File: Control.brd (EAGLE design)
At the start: 93.7 x 34.3 mm, 23 parts, among them IC1 MEGA8-P, Q1 16MHz, T1 2N2222, X1 MKDSN1,5/3-5,08, X2 MKDSN1,5/3-5,08

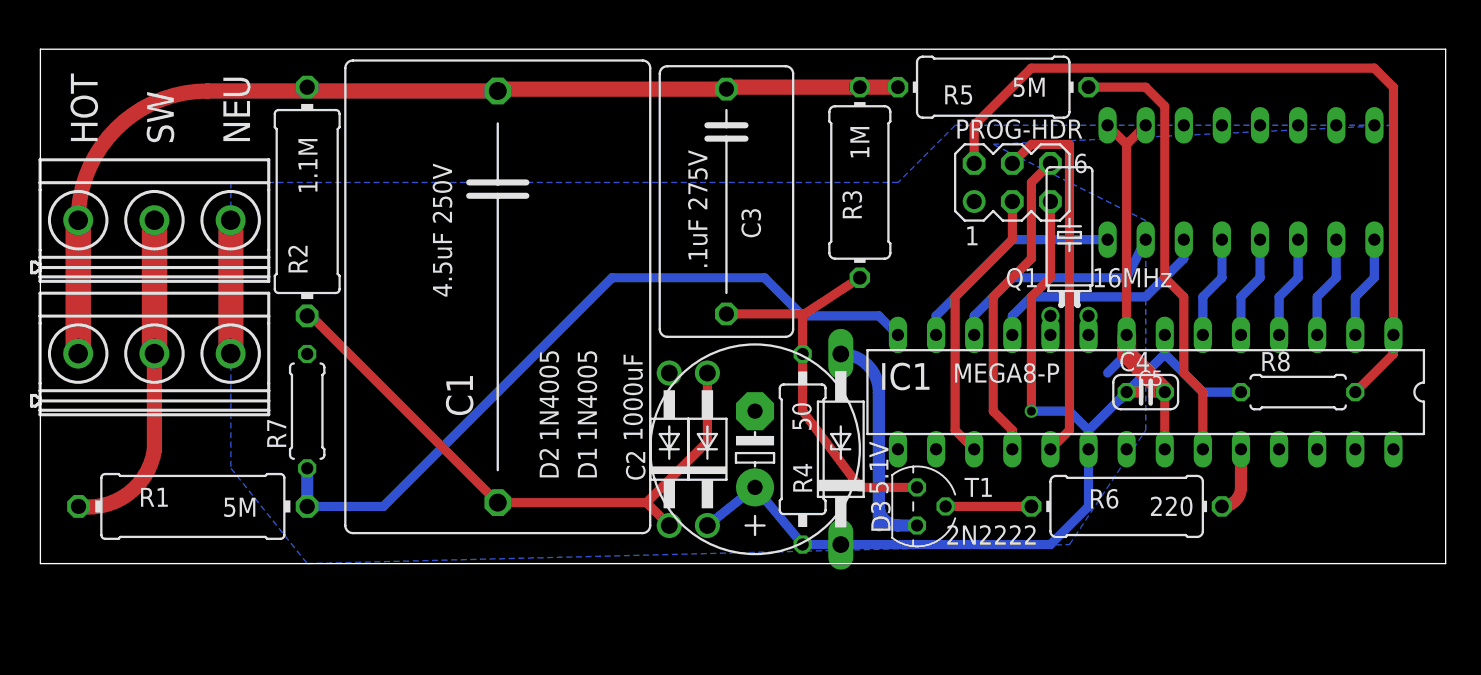
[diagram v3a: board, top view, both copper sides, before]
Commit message: Added surface mount options for low voltage section
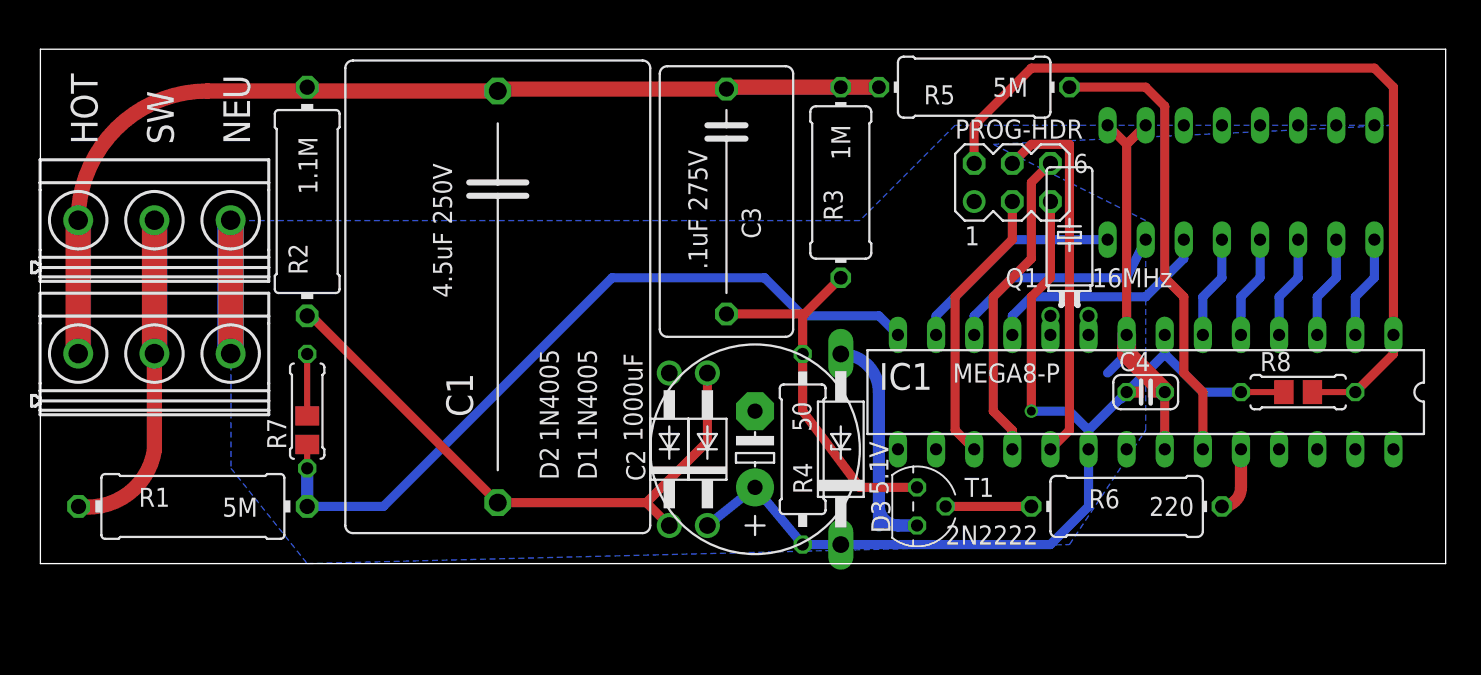
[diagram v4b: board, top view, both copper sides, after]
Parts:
- added R10, R9: 120K, rcl:M0805
- moved R3 1.27 mm to (59.7, 25.4)
- moved R5 1.27 mm to (68.6, 31.8)
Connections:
- net +5V: now also R9.1
- net GND: now also R10.2
- net N$18: now also R10.1
- net N$8: now also R9.2
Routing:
- net GND: track 43.6 -> 56.6 mm
- net N$8: track 54.0 -> 56.8 mm
- net +5V: track 68.5 -> 71.4 mm
- net N$18: track 49.8 -> 51.4 mm
- net N$3: track 67.2 -> 65.9 mm
- net N$21: track 29.5 -> 30.8 mm
- net N$19: track 26.2 -> 25.3 mm
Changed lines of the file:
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@@
 <attribute name="VALUE" x="66.675" y="1.27" size="1.27" layer="25" ratio="10"/>
 </element>
-<element name="R3" library="rcl" package="0411/12" value="1M" x="60.96" y="25.4" smashed="yes" rot="R90">
-<attribute name="NAME" x="61.087" y="22.86" size="1.27" layer="25" ratio="10" rot="R90"/>
-<attribute name="VALUE" x="61.595" y="26.8986" size="1.27" layer="25" ratio="10" rot="R90"/>
+<element name="R3" library="rcl" package="0411/12" value="1M" x="59.69" y="25.4" smashed="yes" rot="R90">
+<attribute name="NAME" x="59.817" y="22.86" size="1.27" layer="25" ratio="10" rot="R90"/>
+<attribute name="VALUE" x="60.325" y="26.8986" size="1.27" layer="25" ratio="10" rot="R90"/>
 </element>
 <element name="R4" library="rcl" package="0309/12" value="50" x="57.15" y="7.62" smashed="yes" rot="R270">
@@
 <attribute name="VALUE" x="56.4642" y="10.795" size="1.27" layer="25" ratio="10" rot="R270"/>
 </element>
-<element name="R5" library="rcl" package="0411/12" value="5M" x="69.85" y="31.75" smashed="yes" rot="R180">
-<attribute name="NAME" x="68.58" y="31.877" size="1.27" layer="25" ratio="10" rot="R180"/>
-<attribute name="VALUE" x="73.4314" y="32.385" size="1.27" layer="25" ratio="10" rot="R180"/>
+<element name="R5" library="rcl" package="0411/12" value="5M" x="68.58" y="31.75" smashed="yes" rot="R180">
+<attribute name="NAME" x="67.31" y="31.877" size="1.27" layer="25" ratio="10" rot="R180"/>
+<attribute name="VALUE" x="72.1614" y="32.385" size="1.27" layer="25" ratio="10" rot="R180"/>
 </element>
 <element name="C3" library="rcl" package="C150-091X182" value=".1uF 275V" x="52.07" y="24.13" smashed="yes" rot="R270">
@@
 </element>
 <element name="C4" library="rcl" package="C025-024X044" value="" x="80.01" y="11.43"/>
-<element name="R7" library="rcl" package="0207/7" value="120K" x="24.13" y="10.16" rot="R90"/>
+<element name="R7" library="rcl" package="0207/7" value="120K" x="24.13" y="10.16" smashed="yes" rot="R90">
+<attribute name="NAME" x="22.733" y="7.62" size="1.27" layer="25" ratio="10" rot="R90"/>
+</element>
 <element name="R8" library="rcl" package="0207/7" value="120K" x="90.17" y="11.43" smashed="yes">
 <attribute name="NAME" x="87.63" y="12.827" size="1.27" layer="25" ratio="10"/>
-<attribute name="VALUE" x="87.884" y="10.8712" size="1.27" layer="27" ratio="10"/>
-</element>
-<element name="C5" library="rcl" package="C0402K" value="" x="80.01" y="11.43"/>
+<attribute name="VALUE" x="87.884" y="8.89" size="1.27" layer="27" ratio="10"/>
+</element>
+<element name="C5" library="rcl" package="C0402K" value="" x="80.01" y="11.43" smashed="yes">
+<attribute name="VALUE" x="79.51" y="9.98" size="1.016" layer="27"/>
+</element>
+<element name="R9" library="rcl" package="M0805" value="120K" x="90.17" y="11.43" smashed="yes"/>
+<element name="R10" library="rcl" package="M0805" value="120K" x="24.13" y="8.89" smashed="yes" rot="R90">
+<attribute name="VALUE" x="26.67" y="7.62" size="1.27" layer="27" rot="R90"/>
+</element>
 </elements>
 <signals>
@@
 <wire x1="81.28" y1="7.62" x2="81.28" y2="11.43" width="0.6096" layer="1"/>
 <polygon width="1.016" layer="16" isolate="0.6096">
-<vertex x="19.05" y="25.4"/>
+<vertex x="19.05" y="22.86"/>
 <vertex x="19.05" y="6.35"/>
 <vertex x="24.13" y="0"/>
@@
 <vertex x="96.52" y="29.21"/>
 <vertex x="67.31" y="29.21"/>
-<vertex x="63.5" y="25.4"/>
+<vertex x="60.96" y="22.86"/>
 </polygon>
 <wire x1="78.74" y1="15.24" x2="78.74" y2="13.97" width="0.6096" layer="16"/>
@@
 <wire x1="78.74" y1="27.94" x2="80.01" y2="29.21" width="0.6096" layer="1"/>
 <contactref element="C5" pad="2"/>
+<wire x1="19.0289" y1="22.885" x2="19.0289" y2="13.995" width="1.778" layer="16"/>
+<contactref element="R10" pad="2"/>
+<wire x1="24.13" y1="9.84" x2="24.13" y2="13.97" width="0.4064" layer="1"/>
 <wire x1="81.28" y1="11.43" x2="80.61" y2="11.43" width="0" layer="19" extent="1-1"/>
 </signal>
@@
 <wire x1="93.98" y1="11.43" x2="96.52" y2="13.97" width="0.6096" layer="1"/>
 <wire x1="96.52" y1="13.97" x2="96.52" y2="15.24" width="0.6096" layer="1"/>
+<contactref element="R9" pad="2"/>
+<wire x1="91.12" y1="11.43" x2="93.98" y2="11.43" width="0.4064" layer="1"/>
 </signal>
 <signal name="+5V">
@@
 <wire x1="83.82" y1="11.43" x2="81.28" y2="13.97" width="0.6096" layer="16"/>
 <contactref element="C5" pad="1"/>
-<wire x1="78.74" y1="11.43" x2="79.41" y2="11.43" width="0" layer="19" extent="1-16"/>
+<contactref element="R9" pad="1"/>
+<wire x1="79.41" y1="11.43" x2="78.74" y2="11.43" width="0" layer="19" extent="1-16"/>
+<wire x1="86.36" y1="11.43" x2="89.22" y2="11.43" width="0.4064" layer="1"/>
 </signal>
 <signal name="N$9">
@@
 <contactref element="R7" pad="1"/>
 <wire x1="24.13" y1="3.81" x2="24.13" y2="6.35" width="0.8128" layer="16"/>
+<contactref element="R10" pad="1"/>
+<wire x1="24.13" y1="7.94" x2="24.13" y2="6.35" width="0.4064" layer="1"/>
 </signal>
 <signal name="N$19">
@@
 <wire x1="52.07" y1="16.637" x2="57.15" y2="16.637" width="0.6096" layer="1"/>
 <wire x1="57.15" y1="16.637" x2="57.277" y2="16.637" width="0.6096" layer="1"/>
-<wire x1="57.277" y1="16.637" x2="60.96" y2="19.05" width="0.6096" layer="1"/>
+<wire x1="57.277" y1="16.637" x2="59.69" y2="19.05" width="0.6096" layer="1"/>
 <wire x1="57.15" y1="13.97" x2="57.15" y2="16.637" width="0.6096" layer="1"/>
 <wire x1="57.15" y1="13.97" x2="57.15" y2="10.16" width="0.6096" layer="1"/>
@@
 <wire x1="36.957" y1="31.623" x2="52.07" y2="31.623" width="1.016" layer="1"/>
 <wire x1="52.07" y1="31.623" x2="52.197" y2="31.75" width="1.016" layer="1"/>
-<wire x1="52.197" y1="31.75" x2="60.96" y2="31.75" width="1.016" layer="1"/>
-<wire x1="60.96" y1="31.75" x2="63.5" y2="31.75" width="1.016" layer="1"/>
+<wire x1="52.197" y1="31.75" x2="59.69" y2="31.75" width="1.016" layer="1"/>
+<wire x1="59.69" y1="31.75" x2="62.23" y2="31.75" width="1.016" layer="1"/>
 <wire x1="17.4799" y1="31.496" x2="8.8689" y2="22.885" width="1.016" layer="1" curve="90"/>
 <wire x1="8.8689" y1="22.885" x2="8.8689" y2="13.995" width="1.6764" layer="1"/>
@@
 <wire x1="81.28" y1="19.05" x2="81.28" y2="30.48" width="0.6096" layer="1"/>
 <wire x1="81.28" y1="30.48" x2="80.01" y2="31.75" width="0.6096" layer="1"/>
-<wire x1="80.01" y1="31.75" x2="76.2" y2="31.75" width="0.6096" layer="1"/>
+<wire x1="80.01" y1="31.75" x2="74.93" y2="31.75" width="0.6096" layer="1"/>
 </signal>
 <signal name="N$22">

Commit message: Updated board - relocated programming header and large filter capacitor from DC block due to assembly dificulties stacking the filter capacitor on top of the diodes.
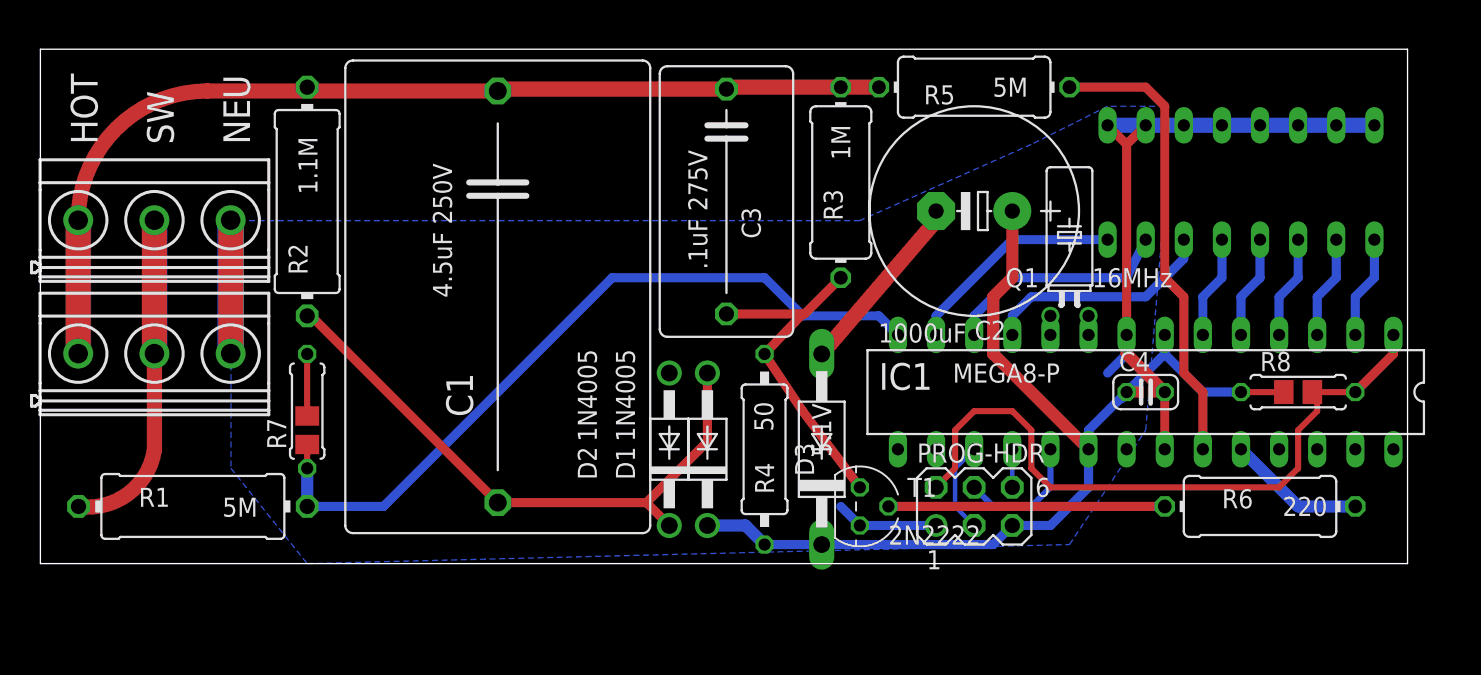
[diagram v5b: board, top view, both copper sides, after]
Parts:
- moved PROG-HDR 21.7 mm to (68.6, 3.81)
- moved C2 21.6 mm to (68.6, 23.5), turned to 180 degrees
- moved R6 8.89 mm to (87.6, 3.81)
- moved T1 3.81 mm to (61.0, 3.81)
- moved R4 2.54 mm to (54.6, 7.62)
- moved D3 1.27 mm to (58.4, 7.62)
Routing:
- net GND: track 56.6 -> 77.4 mm
- net N$6: track 21.2 -> 2.54 mm
- net N$7: track 25.2 -> 8.67 mm
- net N$5: track 5.72 -> 18.4 mm
- net N$9: track 18.6 -> 6.13 mm
- net N$8: track 56.8 -> 45.3 mm
- net N$22: track 4.34 -> 9.20 mm
- net +5V: track 71.4 -> 68.7 mm, vias 1 -> 0
- net N$19: track 25.3 -> 23.2 mm
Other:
- board size 93.7 x 34.3 mm -> 91.1 x 34.3 mm

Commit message: Slight board size reduction
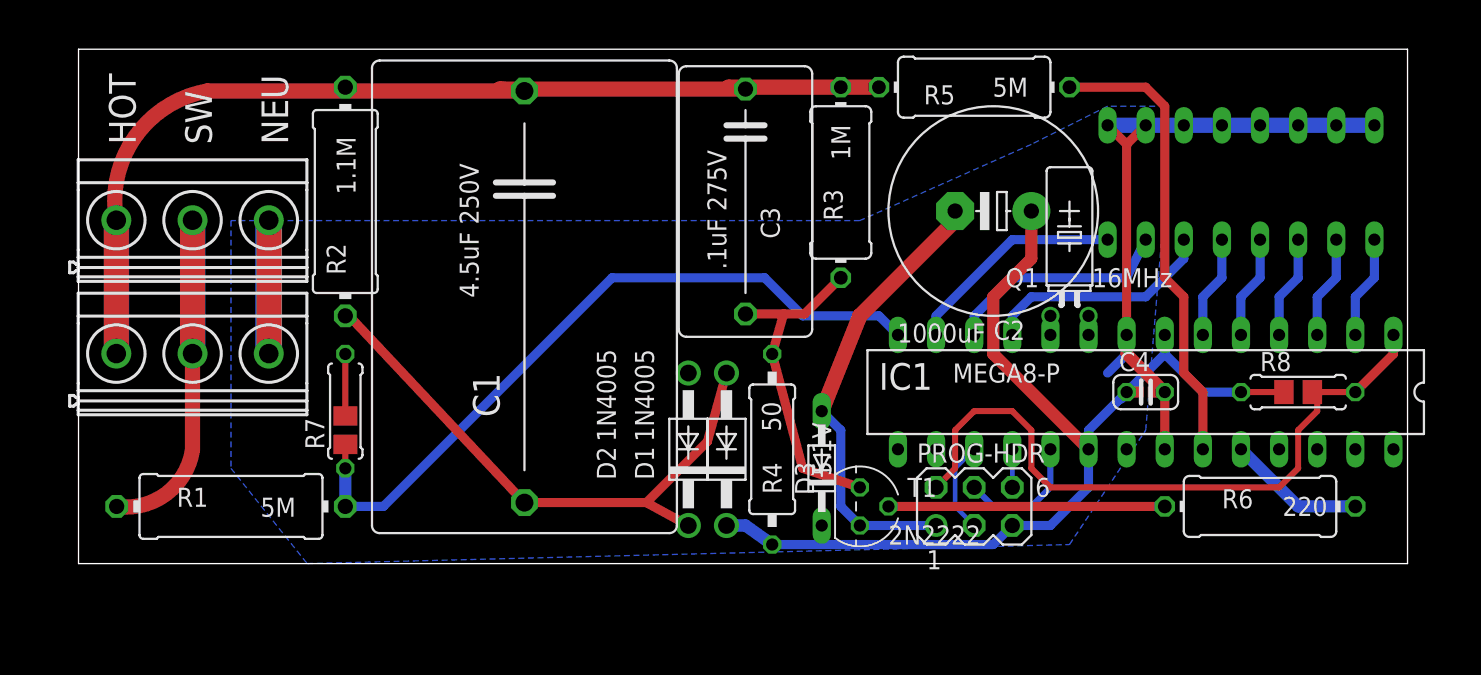
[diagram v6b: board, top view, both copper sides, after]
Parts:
- D3: device diode:P1Z12 -> diode:DO34Z7
- moved R10 2.54 mm to (26.7, 8.89)
- moved R2 2.54 mm to (26.7, 24.1)
- moved R7 2.54 mm to (26.7, 10.2)
- moved R1 2.54 mm to (19.1, 3.81)
- moved X1 2.54 mm to (19.1, 14.0)
- moved X2 2.54 mm to (19.1, 22.9)
- moved C1 1.78 mm to (38.6, 17.8)
- moved C3 1.27 mm to (53.3, 24.1)
- moved D1 1.27 mm to (52.1, 7.62)
- moved D2 1.27 mm to (49.5, 7.62)
- moved D3 1.27 mm to (58.4, 6.35)
- moved C2 1.27 mm to (69.8, 23.5)
- moved R4 0.51 mm to (55.1, 7.62)
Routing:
- net GND: track 77.4 -> 88.4 mm
- net N$3: track 65.9 -> 69.8 mm
- net N$18: track 51.4 -> 48.9 mm
- net N$19: track 23.2 -> 22.0 mm
- net N$4: track 40.2 -> 39.1 mm
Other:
- board size 91.1 x 34.3 mm -> 88.6 x 34.3 mm
